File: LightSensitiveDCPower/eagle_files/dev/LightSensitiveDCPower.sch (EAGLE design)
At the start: 5 parts, among them SW1 PCM12SMTR

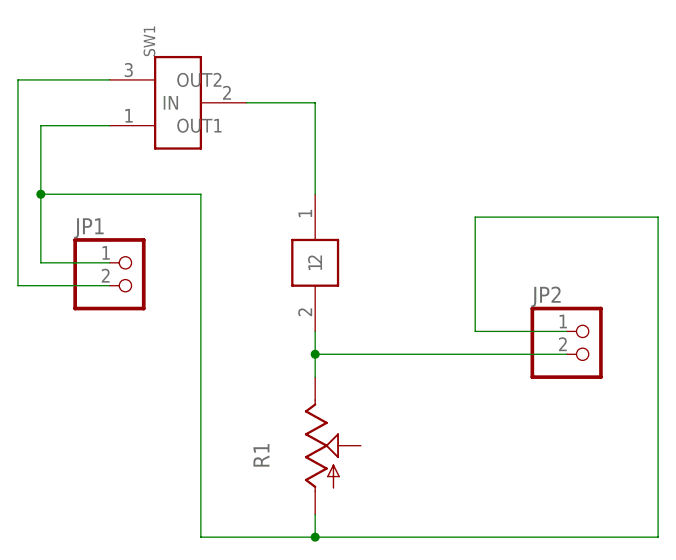
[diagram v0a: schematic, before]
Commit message: Re-place parts with readjusted text and new labels
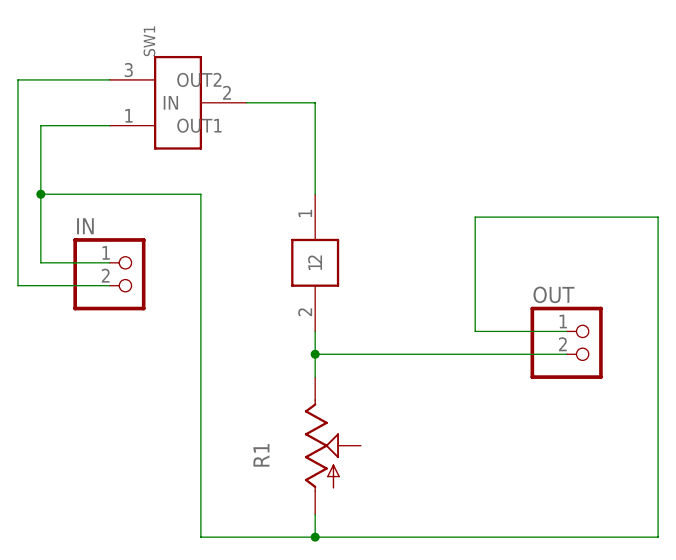
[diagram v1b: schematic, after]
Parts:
- renumbered JP1 to IN, JP2 to OUT
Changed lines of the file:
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@@
 <part name="SW1" library="freddyLibr" deviceset="PCM12SMTR" device=""/>
 <part name="R1" library="pot" deviceset="TRIM_US-" device="B25P"/>
-<part name="JP1" library="pinhead" deviceset="PINHD-1X2" device=""/>
-<part name="JP2" library="pinhead" deviceset="PINHD-1X2" device=""/>
+<part name="IN" library="pinhead" deviceset="PINHD-1X2" device=""/>
+<part name="OUT" library="pinhead" deviceset="PINHD-1X2" device=""/>
 </parts>
 <sheets>
@@
 <instance part="SW1" gate="G$1" x="-10.16" y="71.12" rot="R90"/>
 <instance part="R1" gate="G$1" x="5.08" y="33.02"/>
-<instance part="JP1" gate="G$1" x="-15.24" y="50.8"/>
-<instance part="JP2" gate="G$1" x="35.56" y="43.18"/>
+<instance part="IN" gate="G$1" x="-15.24" y="50.8"/>
+<instance part="OUT" gate="G$1" x="35.56" y="43.18"/>
 </instances>
 <busses>
@@
 <net name="N$1" class="0">
 <segment>
-<pinref part="JP1" gate="G$1" pin="1"/>
+<pinref part="IN" gate="G$1" pin="1"/>
 <wire x1="-17.78" y1="53.34" x2="-25.4" y2="53.34" width="0.1524" layer="91"/>
 <wire x1="-25.4" y1="53.34" x2="-25.4" y2="60.96" width="0.1524" layer="91"/>
@@
 <wire x1="-7.62" y1="60.96" x2="-25.4" y2="60.96" width="0.1524" layer="91"/>
 <junction x="-25.4" y="60.96"/>
-<pinref part="JP2" gate="G$1" pin="1"/>
+<pinref part="OUT" gate="G$1" pin="1"/>
 <wire x1="33.02" y1="45.72" x2="22.86" y2="45.72" width="0.1524" layer="91"/>
 <wire x1="22.86" y1="45.72" x2="22.86" y2="58.42" width="0.1524" layer="91"/>
@@
 <net name="N$2" class="0">
 <segment>
-<pinref part="JP1" gate="G$1" pin="2"/>
+<pinref part="IN" gate="G$1" pin="2"/>
 <wire x1="-17.78" y1="50.8" x2="-27.94" y2="50.8" width="0.1524" layer="91"/>
 <wire x1="-27.94" y1="50.8" x2="-27.94" y2="73.66" width="0.1524" layer="91"/>
@@
 <pinref part="R1" gate="G$1" pin="E"/>
 <wire x1="5.08" y1="45.72" x2="5.08" y2="43.18" width="0.1524" layer="91"/>
-<pinref part="JP2" gate="G$1" pin="2"/>
+<pinref part="OUT" gate="G$1" pin="2"/>
 <wire x1="5.08" y1="43.18" x2="5.08" y2="40.64" width="0.1524" layer="91"/>
 <wire x1="33.02" y1="43.18" x2="5.08" y2="43.18" width="0.1524" layer="91"/>

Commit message: Corrected Pot miswiring. Further rearranging and resizing. I think this is it.
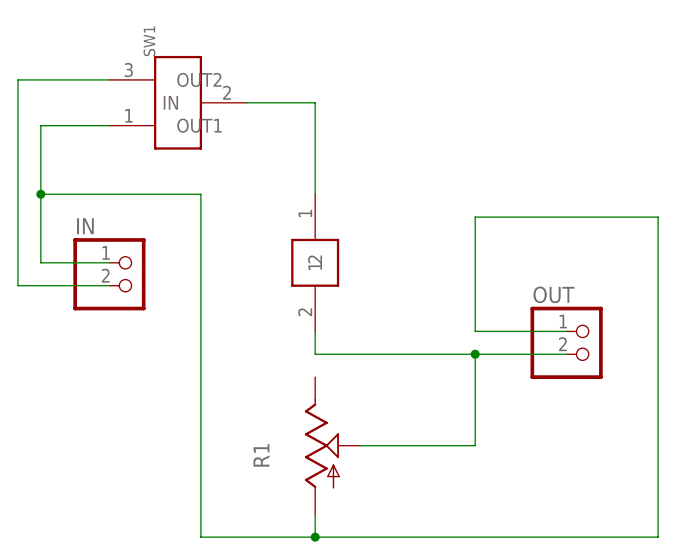
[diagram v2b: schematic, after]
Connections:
- removed net N$5: OUT.2, PC1.2, R1.E
- new net N$4: OUT.2, PC1.2, R1.S
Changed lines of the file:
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@@
 </segment>
 </net>
-<net name="N$5" class="0">
+<net name="N$4" class="0">
 <segment>
+<pinref part="R1" gate="G$1" pin="S"/>
+<wire x1="10.16" y1="33.02" x2="22.86" y2="33.02" width="0.1524" layer="91"/>
+<wire x1="22.86" y1="33.02" x2="22.86" y2="43.18" width="0.1524" layer="91"/>
+<pinref part="OUT" gate="G$1" pin="2"/>
+<wire x1="22.86" y1="43.18" x2="33.02" y2="43.18" width="0.1524" layer="91"/>
 <pinref part="PC1" gate="G$1" pin="2"/>
-<pinref part="R1" gate="G$1" pin="E"/>
 <wire x1="5.08" y1="45.72" x2="5.08" y2="43.18" width="0.1524" layer="91"/>
-<pinref part="OUT" gate="G$1" pin="2"/>
-<wire x1="5.08" y1="43.18" x2="5.08" y2="40.64" width="0.1524" layer="91"/>
-<wire x1="33.02" y1="43.18" x2="5.08" y2="43.18" width="0.1524" layer="91"/>
-<junction x="5.08" y="43.18"/>
+<wire x1="5.08" y1="43.18" x2="22.86" y2="43.18" width="0.1524" layer="91"/>
+<junction x="22.86" y="43.18"/>
 </segment>
 </net>
